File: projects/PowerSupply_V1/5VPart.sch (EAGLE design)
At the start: 15 parts, among them IC1 LM2596T, IC2 LM2991, X1 IN

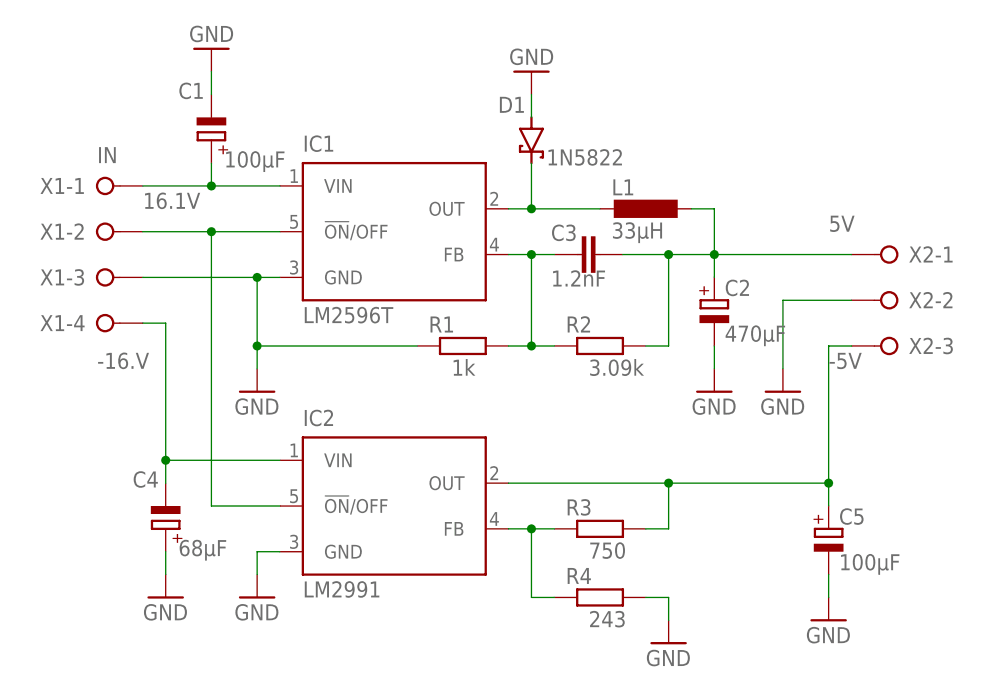
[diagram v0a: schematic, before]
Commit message: feat: power supply
changes:
- version one done
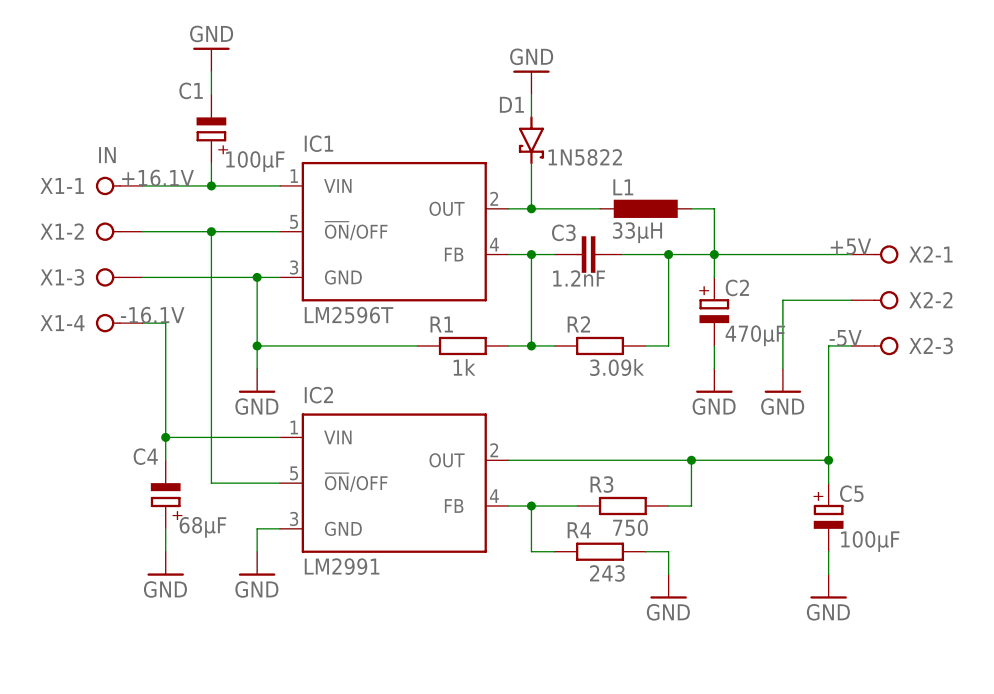
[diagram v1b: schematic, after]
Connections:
- net -16.V renamed -16.1V
- net 16.1V renamed +16.1V
- net 5V renamed +5V
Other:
- moved on the sheet: C4, C5, IC2, R3, R4
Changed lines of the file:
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@@
 <attribute name="NAME" x="171.45" y="99.949" size="1.778" layer="95" rot="MR180"/>
 </instance>
-<instance part="IC2" gate="G$1" x="114.3" y="81.28" smashed="yes">
-<attribute name="NAME" x="104.14" y="90.17" size="1.778" layer="95"/>
-<attribute name="VALUE" x="104.14" y="71.12" size="1.778" layer="96"/>
-</instance>
-<instance part="GND5" gate="1" x="99.06" y="71.12" smashed="yes">
-<attribute name="VALUE" x="96.52" y="68.58" size="1.778" layer="96"/>
-</instance>
-<instance part="C4" gate="G$1" x="88.9" y="78.74" smashed="yes" rot="R180">
-<attribute name="NAME" x="85.217" y="83.3374" size="1.778" layer="95"/>
-<attribute name="VALUE" x="90.297" y="75.7174" size="1.778" layer="96"/>
-</instance>
-<instance part="GND6" gate="1" x="88.9" y="71.12" smashed="yes">
-<attribute name="VALUE" x="86.36" y="68.58" size="1.778" layer="96"/>
-</instance>
-<instance part="C5" gate="G$1" x="162.56" y="78.74" smashed="yes">
-<attribute name="NAME" x="163.703" y="79.2226" size="1.778" layer="95"/>
-<attribute name="VALUE" x="163.703" y="74.1426" size="1.778" layer="96"/>
-</instance>
-<instance part="GND7" gate="1" x="162.56" y="68.58" smashed="yes">
-<attribute name="VALUE" x="160.02" y="66.04" size="1.778" layer="96"/>
-</instance>
-<instance part="R3" gate="G$1" x="137.16" y="78.74" smashed="yes">
-<attribute name="NAME" x="133.35" y="80.2386" size="1.778" layer="95"/>
-<attribute name="VALUE" x="135.89" y="75.438" size="1.778" layer="96"/>
-</instance>
-<instance part="R4" gate="G$1" x="137.16" y="71.12" smashed="yes">
-<attribute name="NAME" x="133.35" y="72.6186" size="1.778" layer="95"/>
-<attribute name="VALUE" x="135.89" y="67.818" size="1.778" layer="96"/>
-</instance>
-<instance part="GND9" gate="1" x="144.78" y="66.04" smashed="yes">
-<attribute name="VALUE" x="142.24" y="63.5" size="1.778" layer="96"/>
+<instance part="IC2" gate="G$1" x="114.3" y="83.82" smashed="yes">
+<attribute name="NAME" x="104.14" y="92.71" size="1.778" layer="95"/>
+<attribute name="VALUE" x="104.14" y="73.66" size="1.778" layer="96"/>
+</instance>
+<instance part="GND5" gate="1" x="99.06" y="73.66" smashed="yes">
+<attribute name="VALUE" x="96.52" y="71.12" size="1.778" layer="96"/>
+</instance>
+<instance part="C4" gate="G$1" x="88.9" y="81.28" smashed="yes" rot="R180">
+<attribute name="NAME" x="85.217" y="85.8774" size="1.778" layer="95"/>
+<attribute name="VALUE" x="90.297" y="78.2574" size="1.778" layer="96"/>
+</instance>
+<instance part="GND6" gate="1" x="88.9" y="73.66" smashed="yes">
+<attribute name="VALUE" x="86.36" y="71.12" size="1.778" layer="96"/>
+</instance>
+<instance part="C5" gate="G$1" x="162.56" y="81.28" smashed="yes">
+<attribute name="NAME" x="163.703" y="81.7626" size="1.778" layer="95"/>
+<attribute name="VALUE" x="163.703" y="76.6826" size="1.778" layer="96"/>
+</instance>
+<instance part="GND7" gate="1" x="162.56" y="71.12" smashed="yes">
+<attribute name="VALUE" x="160.02" y="68.58" size="1.778" layer="96"/>
+</instance>
+<instance part="R3" gate="G$1" x="139.7" y="81.28" smashed="yes">
+<attribute name="NAME" x="135.89" y="82.7786" size="1.778" layer="95"/>
+<attribute name="VALUE" x="138.43" y="77.978" size="1.778" layer="96"/>
+</instance>
+<instance part="R4" gate="G$1" x="137.16" y="76.2" smashed="yes">
+<attribute name="NAME" x="133.35" y="77.6986" size="1.778" layer="95"/>
+<attribute name="VALUE" x="135.89" y="72.898" size="1.778" layer="96"/>
+</instance>
+<instance part="GND9" gate="1" x="144.78" y="71.12" smashed="yes">
+<attribute name="VALUE" x="142.24" y="68.58" size="1.778" layer="96"/>
 </instance>
 </instances>
@@
 <segment>
 <pinref part="IC2" gate="G$1" pin="GND"/>
-<wire x1="101.6" y1="76.2" x2="99.06" y2="76.2" width="0.1524" layer="91"/>
+<wire x1="101.6" y1="78.74" x2="99.06" y2="78.74" width="0.1524" layer="91"/>
 <pinref part="GND5" gate="1" pin="GND"/>
-<wire x1="99.06" y1="76.2" x2="99.06" y2="73.66" width="0.1524" layer="91"/>
+<wire x1="99.06" y1="78.74" x2="99.06" y2="76.2" width="0.1524" layer="91"/>
 </segment>
 <segment>
 <pinref part="C4" gate="G$1" pin="+"/>
 <pinref part="GND6" gate="1" pin="GND"/>
-<wire x1="88.9" y1="76.2" x2="88.9" y2="73.66" width="0.1524" layer="91"/>
+<wire x1="88.9" y1="78.74" x2="88.9" y2="76.2" width="0.1524" layer="91"/>
 </segment>
 <segment>
 <pinref part="C5" gate="G$1" pin="-"/>
 <pinref part="GND7" gate="1" pin="GND"/>
-<wire x1="162.56" y1="73.66" x2="162.56" y2="71.12" width="0.1524" layer="91"/>
+<wire x1="162.56" y1="76.2" x2="162.56" y2="73.66" width="0.1524" layer="91"/>
 </segment>
 <segment>
 <pinref part="R4" gate="G$1" pin="2"/>
-<wire x1="142.24" y1="71.12" x2="144.78" y2="71.12" width="0.1524" layer="91"/>
+<wire x1="142.24" y1="76.2" x2="144.78" y2="76.2" width="0.1524" layer="91"/>
 <pinref part="GND9" gate="1" pin="GND"/>
-<wire x1="144.78" y1="71.12" x2="144.78" y2="68.58" width="0.1524" layer="91"/>
+<wire x1="144.78" y1="76.2" x2="144.78" y2="73.66" width="0.1524" layer="91"/>
 </segment>
 </net>
@@
 </segment>
 </net>
-<net name="5V" class="0">
+<net name="+5V" class="0">
 <segment>
 <pinref part="R2" gate="G$1" pin="2"/>
@@
 <pinref part="X2" gate="-1" pin="KL"/>
 <wire x1="149.86" y1="109.22" x2="165.1" y2="109.22" width="0.1524" layer="91"/>
-<label x="162.56" y="111.76" size="1.778" layer="95"/>
+<label x="162.56" y="109.22" size="1.778" layer="95"/>
 </segment>
 </net>
@@
 <pinref part="IC2" gate="G$1" pin="!ON!/OFF"/>
 <wire x1="93.98" y1="111.76" x2="86.36" y2="111.76" width="0.1524" layer="91"/>
-<wire x1="101.6" y1="81.28" x2="93.98" y2="81.28" width="0.1524" layer="91"/>
-<wire x1="93.98" y1="81.28" x2="93.98" y2="111.76" width="0.1524" layer="91"/>
+<wire x1="101.6" y1="83.82" x2="93.98" y2="83.82" width="0.1524" layer="91"/>
+<wire x1="93.98" y1="83.82" x2="93.98" y2="111.76" width="0.1524" layer="91"/>
 <junction x="93.98" y="111.76"/>
 </segment>
 </net>
-<net name="16.1V" class="0">
+<net name="+16.1V" class="0">
 <segment>
 <pinref part="IC1" gate="G$1" pin="VIN"/>
@@
 <junction x="93.98" y="116.84"/>
 <pinref part="X1" gate="-1" pin="KL"/>
-<label x="86.36" y="114.3" size="1.778" layer="95"/>
-</segment>
-</net>
-<net name="-16.V" class="0">
+<label x="83.82" y="116.84" size="1.778" layer="95"/>
+</segment>
+</net>
+<net name="-16.1V" class="0">
 <segment>
 <pinref part="X1" gate="-4" pin="KL"/>
 <wire x1="86.36" y1="101.6" x2="88.9" y2="101.6" width="0.1524" layer="91"/>
-<wire x1="88.9" y1="101.6" x2="88.9" y2="86.36" width="0.1524" layer="91"/>
+<wire x1="88.9" y1="101.6" x2="88.9" y2="88.9" width="0.1524" layer="91"/>
 <pinref part="IC2" gate="G$1" pin="VIN"/>
-<wire x1="88.9" y1="86.36" x2="101.6" y2="86.36" width="0.1524" layer="91"/>
+<wire x1="88.9" y1="88.9" x2="101.6" y2="88.9" width="0.1524" layer="91"/>
 <pinref part="C4" gate="G$1" pin="-"/>
-<wire x1="88.9" y1="83.82" x2="88.9" y2="86.36" width="0.1524" layer="91"/>
-<junction x="88.9" y="86.36"/>
-<label x="81.28" y="96.52" size="1.778" layer="95"/>
+<wire x1="88.9" y1="86.36" x2="88.9" y2="88.9" width="0.1524" layer="91"/>
+<junction x="88.9" y="88.9"/>
+<label x="83.82" y="101.6" size="1.778" layer="95"/>
 </segment>
 </net>
@@
 <pinref part="X2" gate="-3" pin="KL"/>
 <wire x1="165.1" y1="99.06" x2="162.56" y2="99.06" width="0.1524" layer="91"/>
-<wire x1="162.56" y1="99.06" x2="162.56" y2="83.82" width="0.1524" layer="91"/>
+<wire x1="162.56" y1="99.06" x2="162.56" y2="86.36" width="0.1524" layer="91"/>
 <pinref part="IC2" gate="G$1" pin="OUT"/>
-<wire x1="162.56" y1="83.82" x2="144.78" y2="83.82" width="0.1524" layer="91"/>
-<label x="162.56" y="96.52" size="1.778" layer="95"/>
+<wire x1="162.56" y1="86.36" x2="147.32" y2="86.36" width="0.1524" layer="91"/>
+<label x="162.56" y="99.06" size="1.778" layer="95"/>
 <pinref part="C5" gate="G$1" pin="+"/>
-<wire x1="144.78" y1="83.82" x2="127" y2="83.82" width="0.1524" layer="91"/>
-<wire x1="162.56" y1="81.28" x2="162.56" y2="83.82" width="0.1524" layer="91"/>
-<junction x="162.56" y="83.82"/>
+<wire x1="147.32" y1="86.36" x2="127" y2="86.36" width="0.1524" layer="91"/>
+<wire x1="162.56" y1="83.82" x2="162.56" y2="86.36" width="0.1524" layer="91"/>
+<junction x="162.56" y="86.36"/>
 <pinref part="R3" gate="G$1" pin="2"/>
-<wire x1="142.24" y1="78.74" x2="144.78" y2="78.74" width="0.1524" layer="91"/>
-<wire x1="144.78" y1="78.74" x2="144.78" y2="83.82" width="0.1524" layer="91"/>
-<junction x="144.78" y="83.82"/>
+<wire x1="144.78" y1="81.28" x2="147.32" y2="81.28" width="0.1524" layer="91"/>
+<wire x1="147.32" y1="81.28" x2="147.32" y2="86.36" width="0.1524" layer="91"/>
+<junction x="147.32" y="86.36"/>
 </segment>
 </net>
@@
 <pinref part="IC2" gate="G$1" pin="FB"/>
 <pinref part="R3" gate="G$1" pin="1"/>
-<wire x1="127" y1="78.74" x2="129.54" y2="78.74" width="0.1524" layer="91"/>
+<wire x1="127" y1="81.28" x2="129.54" y2="81.28" width="0.1524" layer="91"/>
 <pinref part="R4" gate="G$1" pin="1"/>
-<wire x1="129.54" y1="78.74" x2="132.08" y2="78.74" width="0.1524" layer="91"/>
-<wire x1="132.08" y1="71.12" x2="129.54" y2="71.12" width="0.1524" layer="91"/>
-<wire x1="129.54" y1="71.12" x2="129.54" y2="78.74" width="0.1524" layer="91"/>
-<junction x="129.54" y="78.74"/>
-</segment>
-</net>
+<wire x1="129.54" y1="81.28" x2="134.62" y2="81.28" width="0.1524" layer="91"/>
+<wire x1="132.08" y1="76.2" x2="129.54" y2="76.2" width="0.1524" layer="91"/>
+<wire x1="129.54" y1="76.2" x2="129.54" y2="81.28" width="0.1524" layer="91"/>
+<junction x="129.54" y="81.28"/>
+</segment>
+</net>

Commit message: feat: pwr fixes
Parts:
- C4, C5: device rcl:CPOL-EUE2.5-6 -> rcl:CPOL-EUE2-5
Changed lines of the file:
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@@
 <grid distance="0.1" unitdist="inch" unit="inch" style="lines" multiple="1" display="no" altdistance="0.01" altunitdist="inch" altunit="inch"/>
 <layers>
-<layer number="1" name="Top" color="4" fill="1" visible="no" active="no"/>
-<layer number="16" name="Bottom" color="1" fill="1" visible="no" active="no"/>
-<layer number="17" name="Pads" color="2" fill="1" visible="no" active="no"/>
-<layer number="18" name="Vias" color="2" fill="1" visible="no" active="no"/>
-<layer number="19" name="Unrouted" color="6" fill="1" visible="no" active="no"/>
-<layer number="20" name="Dimension" color="15" fill="1" visible="no" active="no"/>
-<layer number="21" name="tPlace" color="7" fill="1" visible="no" active="no"/>
-<layer number="22" name="bPlace" color="7" fill="1" visible="no" active="no"/>
-<layer number="23" name="tOrigins" color="15" fill="1" visible="no" active="no"/>
-<layer number="24" name="bOrigins" color="15" fill="1" visible="no" active="no"/>
-<layer number="25" name="tNames" color="7" fill="1" visible="no" active="no"/>
-<layer number="26" name="bNames" color="7" fill="1" visible="no" active="no"/>
-<layer number="27" name="tValues" color="7" fill="1" visible="no" active="no"/>
-<layer number="28" name="bValues" color="7" fill="1" visible="no" active="no"/>
+<layer number="1" name="Top" color="4" fill="1" visible="yes" active="no"/>
+<layer number="16" name="Bottom" color="1" fill="1" visible="yes" active="no"/>
+<layer number="17" name="Pads" color="2" fill="1" visible="yes" active="no"/>
+<layer number="18" name="Vias" color="2" fill="1" visible="yes" active="no"/>
+<layer number="19" name="Unrouted" color="6" fill="1" visible="yes" active="no"/>
+<layer number="20" name="Dimension" color="15" fill="1" visible="yes" active="no"/>
+<layer number="21" name="tPlace" color="7" fill="1" visible="yes" active="no"/>
+<layer number="22" name="bPlace" color="7" fill="1" visible="yes" active="no"/>
+<layer number="23" name="tOrigins" color="15" fill="1" visible="yes" active="no"/>
+<layer number="24" name="bOrigins" color="15" fill="1" visible="yes" active="no"/>
+<layer number="25" name="tNames" color="7" fill="1" visible="yes" active="no"/>
+<layer number="26" name="bNames" color="7" fill="1" visible="yes" active="no"/>
+<layer number="27" name="tValues" color="7" fill="1" visible="yes" active="no"/>
+<layer number="28" name="bValues" color="7" fill="1" visible="yes" active="no"/>
 <layer number="29" name="tStop" color="7" fill="3" visible="no" active="no"/>
 <layer number="30" name="bStop" color="7" fill="6" visible="no" active="no"/>
@@
 <layer number="35" name="tGlue" color="7" fill="4" visible="no" active="no"/>
 <layer number="36" name="bGlue" color="7" fill="5" visible="no" active="no"/>
-<layer number="37" name="tTest" color="7" fill="1" visible="no" active="no"/>
-<layer number="38" name="bTest" color="7" fill="1" visible="no" active="no"/>
+<layer number="37" name="tTest" color="7" fill="1" visible="yes" active="no"/>
+<layer number="38" name="bTest" color="7" fill="1" visible="yes" active="no"/>
 <layer number="39" name="tKeepout" color="4" fill="11" visible="no" active="no"/>
 <layer number="40" name="bKeepout" color="1" fill="11" visible="no" active="no"/>
@@
 <layer number="44" name="Drills" color="7" fill="1" visible="no" active="no"/>
 <layer number="45" name="Holes" color="7" fill="1" visible="no" active="no"/>
-<layer number="46" name="Milling" color="3" fill="1" visible="no" active="no"/>
-<layer number="47" name="Measures" color="7" fill="1" visible="no" active="no"/>
-<layer number="48" name="Document" color="7" fill="1" visible="no" active="no"/>
-<layer number="49" name="Reference" color="7" fill="1" visible="no" active="no"/>
-<layer number="51" name="tDocu" color="6" fill="1" visible="no" active="no"/>
-<layer number="52" name="bDocu" color="7" fill="1" visible="no" active="no"/>
+<layer number="46" name="Milling" color="3" fill="1" visible="yes" active="no"/>
+<layer number="47" name="Measures" color="7" fill="1" visible="yes" active="no"/>
+<layer number="48" name="Document" color="7" fill="1" visible="yes" active="no"/>
+<layer number="49" name="Reference" color="7" fill="1" visible="yes" active="no"/>
+<layer number="51" name="tDocu" color="6" fill="1" visible="yes" active="no"/>
+<layer number="52" name="bDocu" color="7" fill="1" visible="yes" active="no"/>
 <layer number="88" name="SimResults" color="9" fill="1" visible="yes" active="yes"/>
 <layer number="89" name="SimProbes" color="9" fill="1" visible="yes" active="yes"/>
@@
 <part name="IC2" library="national-semiconductor" library_urn="urn:adsk.eagle:library:307" deviceset="LM2596" device="T" package3d_urn="urn:adsk.eagle:package:21216/1" value="LM2991"/>
 <part name="GND5" library="supply1" library_urn="urn:adsk.eagle:library:371" deviceset="GND" device=""/>
-<part name="C4" library="rcl" library_urn="urn:adsk.eagle:library:334" deviceset="CPOL-EU" device="E2.5-6" package3d_urn="urn:adsk.eagle:package:23349/1" value="68µF"/>
+<part name="C4" library="rcl" library_urn="urn:adsk.eagle:library:334" deviceset="CPOL-EU" device="E2-5" package3d_urn="urn:adsk.eagle:package:23346/2" value="68µF"/>
 <part name="GND6" library="supply1" library_urn="urn:adsk.eagle:library:371" deviceset="GND" device=""/>
-<part name="C5" library="rcl" library_urn="urn:adsk.eagle:library:334" deviceset="CPOL-EU" device="E2.5-6" package3d_urn="urn:adsk.eagle:package:23349/1" value="100µF"/>
+<part name="C5" library="rcl" library_urn="urn:adsk.eagle:library:334" deviceset="CPOL-EU" device="E2-5" package3d_urn="urn:adsk.eagle:package:23346/2" value="100µF"/>
 <part name="GND7" library="supply1" library_urn="urn:adsk.eagle:library:371" deviceset="GND" device=""/>
 <part name="R3" library="rcl" library_urn="urn:adsk.eagle:library:334" deviceset="R-EU_" device="0207/10" package3d_urn="urn:adsk.eagle:package:23491/2" value="750"/>
